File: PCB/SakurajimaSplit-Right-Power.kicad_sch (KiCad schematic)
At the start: 19 parts, among them J7 USB-C to Right-Half, U8 TLV76733DRVR, U9 USBLC6-2SC6

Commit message: feat(pcb): fine tune pcb layout
- fine tuned pcb layout
- swaped TX and RX pins of right half for better routing
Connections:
- net at J7.A6 (D+), J7.B6 (D+): now also U9.1 (I/O1); no longer U9.3 (I/O2)
- net at J7.A7 (D-), J7.B7 (D-): now also U9.3 (I/O2); no longer U9.1 (I/O1)
- net at JP6.1 (A), TP24.1: now also U9.6 (I/O1); no longer U9.4 (I/O2)
- net at JP5.1 (A), TP23.1: now also U9.4 (I/O2); no longer U9.6 (I/O1)
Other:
- moved on the sheet: JP5, JP6, TP23, TP24
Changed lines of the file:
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@@
 	)
 	(junction
-		(at 135.89 140.97)
+		(at 254 134.62)
 		(diameter 0)
 		(color 0 0 0 0)
 	)
 	(junction
-		(at 254 134.62)
+		(at 135.89 143.51)
 		(diameter 0)
 		(color 0 0 0 0)
 	)
 	(junction
-		(at 156.21 140.97)
+		(at 299.72 134.62)
 		(diameter 0)
 		(color 0 0 0 0)
 	)
 	(junction
-		(at 299.72 134.62)
+		(at 135.89 138.43)
 		(diameter 0)
 		(color 0 0 0 0)
@@
 	)
 	(junction
+		(at 156.21 140.97)
+		(diameter 0)
+		(color 0 0 0 0)
+	)
+	(junction
 		(at 281.94 134.62)
 		(diameter 0)
@@
 	)
 	(junction
-		(at 156.21 138.43)
+		(at 287.02 134.62)
 		(diameter 0)
 		(color 0 0 0 0)
 	)
 	(junction
-		(at 287.02 134.62)
+		(at 156.21 138.43)
 		(diameter 0)
 		(color 0 0 0 0)
@@
 	)
 	(junction
-		(at 135.89 138.43)
-		(diameter 0)
-		(color 0 0 0 0)
-	)
-	(junction
 		(at 233.68 134.62)
 		(diameter 0)
@@
 	(wire
 		(pts
-			(xy 156.21 138.43) (xy 149.86 138.43)
+			(xy 149.86 138.43) (xy 156.21 138.43)
 		)
 		(stroke
@@
 	(wire
 		(pts
-			(xy 172.72 138.43) (xy 156.21 138.43)
+			(xy 194.31 144.78) (xy 199.39 144.78)
 		)
 		(stroke
@@
 	(wire
 		(pts
-			(xy 194.31 144.78) (xy 199.39 144.78)
+			(xy 281.94 121.92) (xy 281.94 134.62)
 		)
 		(stroke
@@
 	(wire
 		(pts
-			(xy 281.94 121.92) (xy 281.94 134.62)
+			(xy 299.72 142.24) (xy 299.72 144.78)
 		)
 		(stroke
@@
 	(wire
 		(pts
-			(xy 299.72 142.24) (xy 299.72 144.78)
+			(xy 135.89 138.43) (xy 137.16 138.43)
 		)
 		(stroke
@@
 	(wire
 		(pts
-			(xy 170.18 140.97) (xy 156.21 140.97)
+			(xy 156.21 140.97) (xy 170.18 140.97)
 		)
 		(stroke
@@
 	(wire
 		(pts
-			(xy 135.89 138.43) (xy 139.7 138.43)
+			(xy 170.18 147.32) (xy 186.69 147.32)
 		)
 		(stroke
@@
 	(wire
 		(pts
-			(xy 170.18 147.32) (xy 186.69 147.32)
+			(xy 299.72 134.62) (xy 299.72 137.16)
 		)
 		(stroke
@@
 	(wire
 		(pts
-			(xy 299.72 134.62) (xy 299.72 137.16)
+			(xy 194.31 134.62) (xy 224.79 134.62)
 		)
 		(stroke
@@
 	(wire
 		(pts
-			(xy 194.31 134.62) (xy 224.79 134.62)
+			(xy 156.21 138.43) (xy 172.72 138.43)
 		)
 		(stroke
@@
 	(wire
 		(pts
+			(xy 137.16 140.97) (xy 139.7 140.97)
+		)
+		(stroke
+			(width 0)
+			(type default)
+		)
+	)
+	(wire
+		(pts
 			(xy 247.65 134.62) (xy 250.19 134.62)
 		)
@@
 	(wire
 		(pts
+			(xy 135.89 143.51) (xy 138.43 143.51)
+		)
+		(stroke
+			(width 0)
+			(type default)
+		)
+	)
+	(wire
+		(pts
 			(xy 287.02 144.78) (xy 287.02 147.32)
 		)
@@
 	(wire
 		(pts
-			(xy 144.78 123.19) (xy 144.78 133.35)
+			(xy 137.16 138.43) (xy 137.16 140.97)
 		)
 		(stroke
@@
 	(wire
 		(pts
-			(xy 233.68 134.62) (xy 240.03 134.62)
+			(xy 144.78 123.19) (xy 144.78 133.35)
 		)
 		(stroke
@@
 	(wire
 		(pts
-			(xy 194.31 147.32) (xy 199.39 147.32)
+			(xy 233.68 134.62) (xy 240.03 134.62)
 		)
 		(stroke
@@
 	(wire
 		(pts
-			(xy 135.89 140.97) (xy 139.7 140.97)
+			(xy 194.31 147.32) (xy 199.39 147.32)
 		)
 		(stroke
@@
 	(wire
 		(pts
+			(xy 138.43 138.43) (xy 139.7 138.43)
+		)
+		(stroke
+			(width 0)
+			(type default)
+		)
+	)
+	(wire
+		(pts
 			(xy 233.68 144.78) (xy 233.68 147.32)
 		)
@@
 		)
 	)
+	(wire
+		(pts
+			(xy 138.43 143.51) (xy 138.43 138.43)
+		)
+		(stroke
+			(width 0)
+			(type default)
+		)
+	)
 	(hierarchical_label "USART_RX"
 		(shape output)
-		(at 199.39 144.78 0)
+		(at 199.39 147.32 0)
 		(effects
 			(font
@@
 	(hierarchical_label "USART_TX"
 		(shape input)
-		(at 199.39 147.32 0)
+		(at 199.39 144.78 0)
 		(effects
 			(font
@@
 	(symbol
 		(lib_id "Jumper:SolderJumper_2_Open")
-		(at 190.5 147.32 0)
-		(mirror x)
+		(at 190.5 144.78 0)
 		(unit 1)
 		(exclude_from_sim no)
@@
 		(dnp no)
 		(property "Reference" "JP6"
-			(at 190.5 153.67 0)
+			(at 190.5 138.43 0)
 			(effects
 				(font
@@
 		)
 		(property "Value" "USART_TX"
-			(at 190.246 151.13 0)
+			(at 190.246 140.97 0)
 			(effects
 				(font
@@
 		)
 		(property "Footprint" "Jumper:SolderJumper-2_P1.3mm_Open_TrianglePad1.0x1.5mm"
-			(at 190.5 147.32 0)
+			(at 190.5 144.78 0)
 			(effects
 				(font
@@
 		)
 		(property "Datasheet" "~"
-			(at 190.5 147.32 0)
+			(at 190.5 144.78 0)
 			(effects
 				(font
@@
 		)
 		(property "Description" "Solder Jumper, 2-pole, open"
-			(at 190.5 147.32 0)
+			(at 190.5 144.78 0)
 			(effects
 				(font
@@
 	(symbol
 		(lib_id "Connector:TestPoint")
-		(at 156.21 138.43 0)
+		(at 156.21 140.97 0)
+		(mirror x)
 		(unit 1)
 		(exclude_from_sim no)
@@
 		(dnp no)
 		(property "Reference" "TP23"
-			(at 157.988 133.858 0)
+			(at 157.988 145.542 0)
 			(effects
 				(font
@@
 		)
 		(property "Value" "USART_RX"
-			(at 157.734 136.398 0)
+			(at 157.734 143.002 0)
 			(effects
 				(font
@@
 		)
 		(property "Footprint" "Hayata_Lib:TestPoint_Pad_Circular_1.3mm"
-			(at 161.29 138.43 0)
+			(at 161.29 140.97 0)
 			(effects
 				(font
@@
 		)
 		(property "Datasheet" "~"
-			(at 161.29 138.43 0)
+			(at 161.29 140.97 0)
 			(effects
 				(font
@@
 		)
 		(property "Description" "test point"
-			(at 156.21 138.43 0)
+			(at 156.21 140.97 0)
 			(effects
 				(font
@@
 	(symbol
 		(lib_id "Connector:TestPoint")
-		(at 156.21 140.97 0)
-		(mirror x)
+		(at 156.21 138.43 0)
 		(unit 1)
 		(exclude_from_sim no)
@@
 		(dnp no)
 		(property "Reference" "TP24"
-			(at 157.988 145.542 0)
+			(at 157.988 133.858 0)
 			(effects
 				(font
@@
 		)
 		(property "Value" "USART_TX"
-			(at 157.734 143.002 0)
+			(at 157.734 136.398 0)
 			(effects
 				(font
@@
 		)
 		(property "Footprint" "Hayata_Lib:TestPoint_Pad_Circular_1.3mm"
-			(at 161.29 140.97 0)
+			(at 161.29 138.43 0)
 			(effects
 				(font
@@
 		)
 		(property "Datasheet" "~"
-			(at 161.29 140.97 0)
+			(at 161.29 138.43 0)
 			(effects
 				(font
@@
 		)
 		(property "Description" "test point"
-			(at 156.21 140.97 0)
+			(at 156.21 138.43 0)
 			(effects
 				(font
@@
 	(symbol
 		(lib_id "Jumper:SolderJumper_2_Open")
-		(at 190.5 144.78 0)
+		(at 190.5 147.32 0)
+		(mirror x)
 		(unit 1)
 		(exclude_from_sim no)
@@
 		(dnp no)
 		(property "Reference" "JP5"
-			(at 190.5 138.43 0)
+			(at 190.5 153.67 0)
 			(effects
 				(font
@@
 		)
 		(property "Value" "USART_RX"
-			(at 190.246 140.97 0)
+			(at 190.246 151.13 0)
 			(effects
 				(font
@@
 		)
 		(property "Footprint" "Jumper:SolderJumper-2_P1.3mm_Open_TrianglePad1.0x1.5mm"
-			(at 190.5 144.78 0)
+			(at 190.5 147.32 0)
 			(effects
 				(font
@@
 		)
 		(property "Datasheet" "~"
-			(at 190.5 144.78 0)
+			(at 190.5 147.32 0)
 			(effects
 				(font
@@
 		)
 		(property "Description" "Solder Jumper, 2-pole, open"
-			(at 190.5 144.78 0)
+			(at 190.5 147.32 0)
 			(effects
 				(font

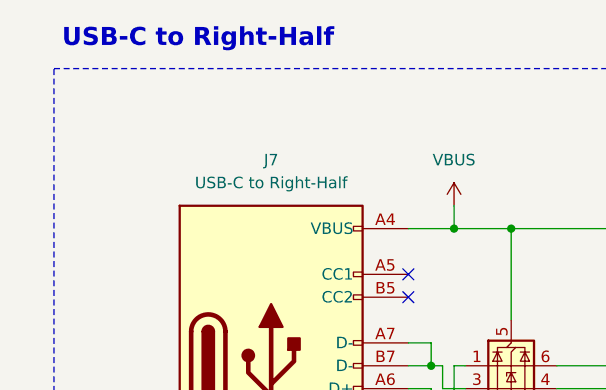
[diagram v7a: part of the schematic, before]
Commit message: feat(pcb): add mounting holes, fix some bugs
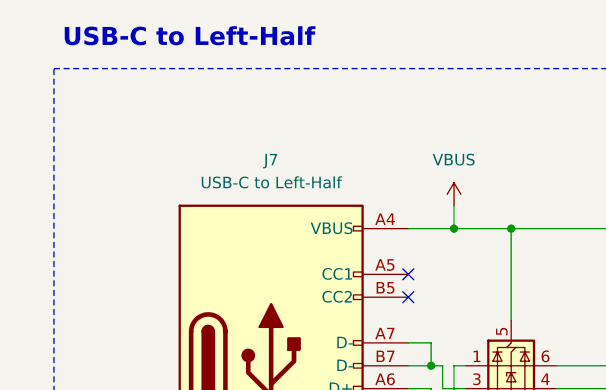
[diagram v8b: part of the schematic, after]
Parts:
- J7: value USB-C to Right-Half -> USB-C to Left-Half
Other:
- note added: "USB-C to Left-Half"
- note removed: "USB-C to Right-Half"
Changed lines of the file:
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@@
 		)
 	)
-	(text "USB-C to Right-Half\n"
+	(text "USB-C to Left-Half\n"
 		(exclude_from_sim no)
-		(at 109.982 102.108 0)
+		(at 108.966 102.108 0)
 		(effects
 			(font
@@
 			)
 		)
-		(property "Value" "USB-C to Right-Half"
+		(property "Value" "USB-C to Left-Half"
 			(at 118.11 118.11 0)
 			(effects
